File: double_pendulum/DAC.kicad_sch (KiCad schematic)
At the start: 16 parts, among them U4 MCP4922-E_P, U5 TL072, U7 MCP4922-E_P, U9 TL072

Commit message: double pendulum 4ms package path update
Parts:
- U5, U9: footprint PCM_4ms_Package_SSOP:TSSOP-8_4.4x3mm_Pitch0.65mm -> 4ms_Package_SSOP:TSSOP-8_4.4x3mm_Pitch0.65mm
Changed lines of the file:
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@@
 			)
 		)
-		(property "Footprint" "PCM_4ms_Package_SSOP:TSSOP-8_4.4x3mm_Pitch0.65mm"
+		(property "Footprint" "4ms_Package_SSOP:TSSOP-8_4.4x3mm_Pitch0.65mm"
 			(at 205.74 33.02 0)
 			(effects
@@
 			)
 		)
-		(property "Footprint" "PCM_4ms_Package_SSOP:TSSOP-8_4.4x3mm_Pitch0.65mm"
+		(property "Footprint" "4ms_Package_SSOP:TSSOP-8_4.4x3mm_Pitch0.65mm"
 			(at 205.74 59.69 0)
 			(effects
@@
 			)
 		)
-		(property "Footprint" "PCM_4ms_Package_SSOP:TSSOP-8_4.4x3mm_Pitch0.65mm"
+		(property "Footprint" "4ms_Package_SSOP:TSSOP-8_4.4x3mm_Pitch0.65mm"
 			(at 204.47 82.55 0)
 			(effects
@@
 			)
 		)
-		(property "Footprint" "PCM_4ms_Package_SSOP:TSSOP-8_4.4x3mm_Pitch0.65mm"
+		(property "Footprint" "4ms_Package_SSOP:TSSOP-8_4.4x3mm_Pitch0.65mm"
 			(at 204.47 109.22 0)
 			(effects

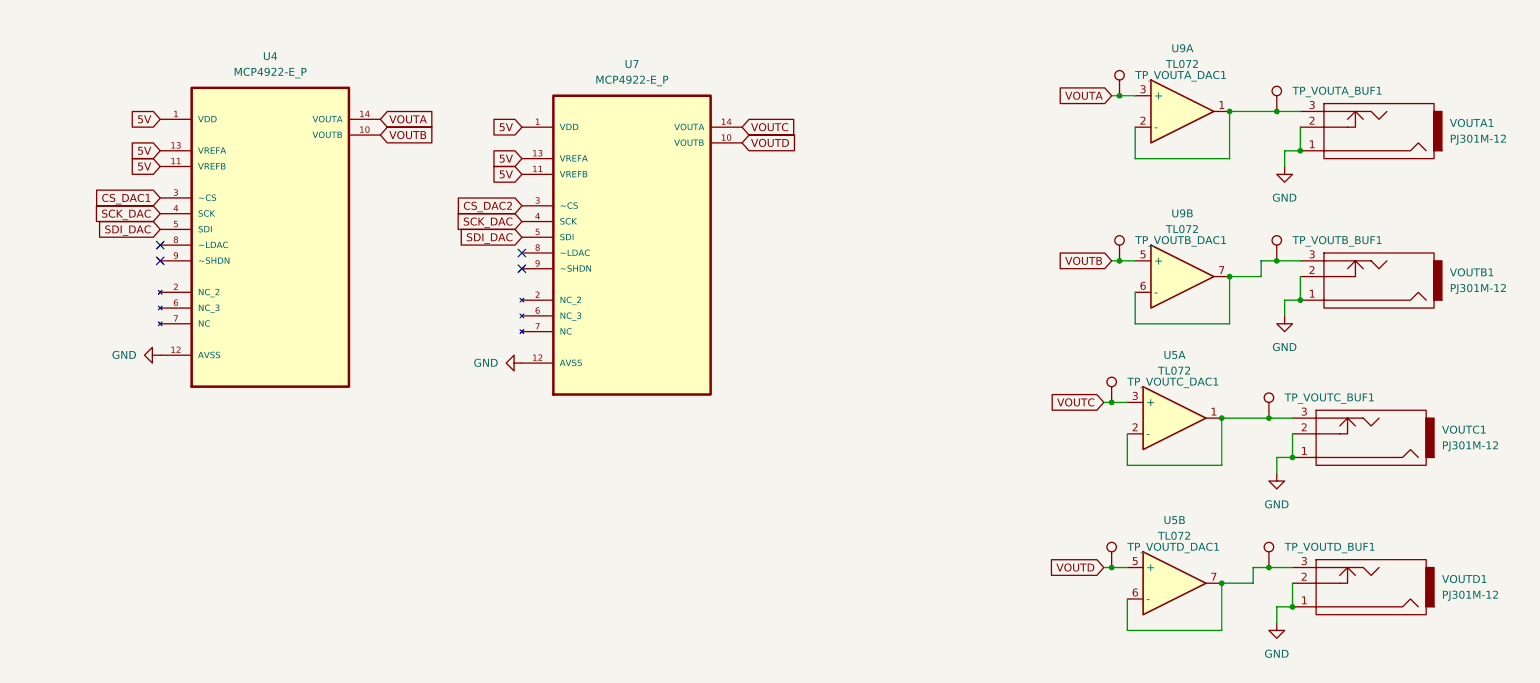
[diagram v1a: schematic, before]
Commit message: Finished schematic and layout of the double pendulum
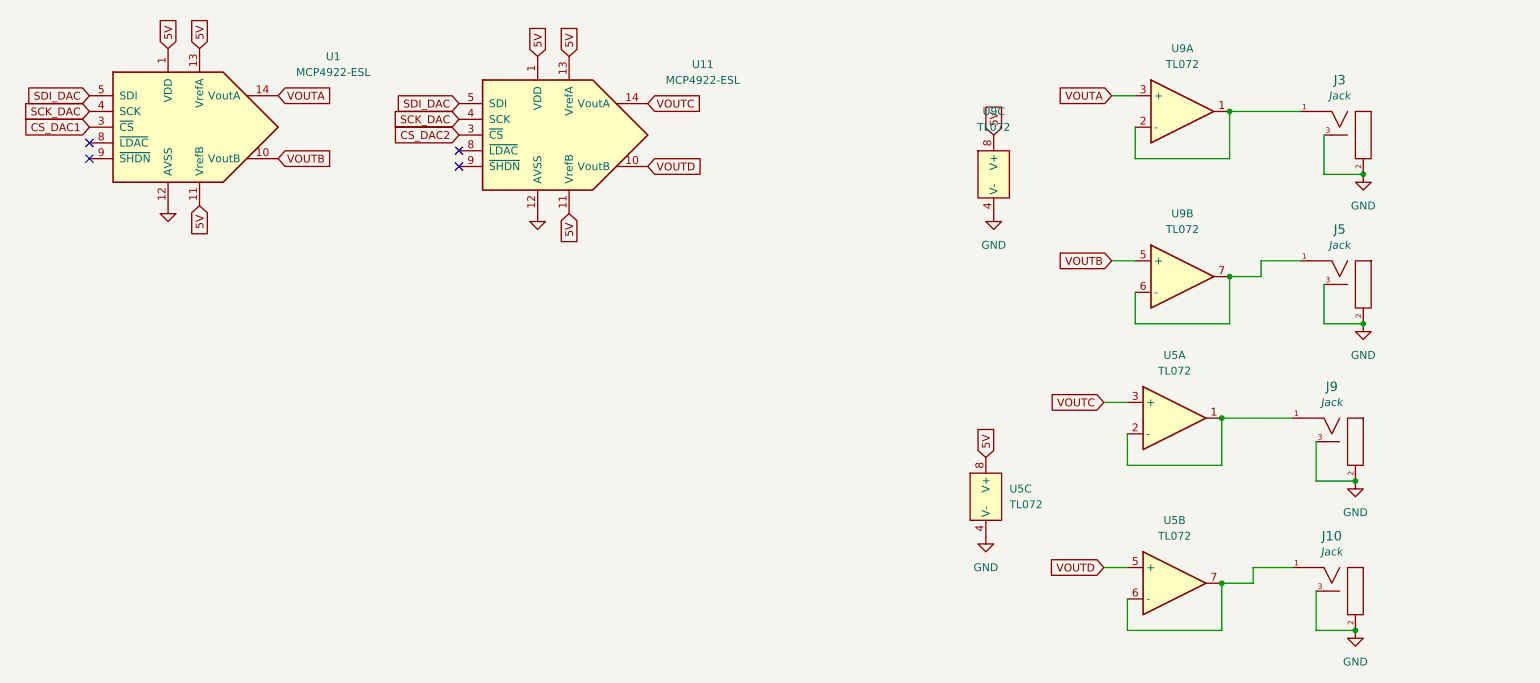
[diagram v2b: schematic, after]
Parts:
- removed TP_VOUTA_BUF1, TP_VOUTA_DAC1, TP_VOUTB_BUF1, TP_VOUTB_DAC1, TP_VOUTC_BUF1, TP_VOUTC_DAC1, TP_VOUTD_BUF1, TP_VOUTD_DAC1: TestPoint, TestPoint:TestPoint_Keystone_5005-5009_Compact, symbol Connector:TestPoint
- removed U4, U7: MCP4922-E_P, MCP4922:DIP254P762X533-14, symbol MCP4922:MCP4922-E_P
- removed VOUTA1, VOUTB1, VOUTC1, VOUTD1: PJ301M-12, Eurocad:PJ301M-12, symbol eurocad:PJ301M-12
- added J10, J3, J5, J9: 3.5mm_Mono_Switched_sm, 4ms_Jack:EighthInch_PJ398SM, symbol 4ms_Jack:3.5mm_Mono_Switched_sm
- added U1, U11: MCP4922-ESL, 4ms_Package_SOIC:SOIC-14_3.9x8.65mm_Pitch1.27mm, symbol Analog_DAC:MCP4922-ESL
- added unit 3 of U5
- added unit 3 of U9
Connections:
- net 5V: now also U1.1 (VDD), U1.11 (VrefB), U1.13 (VrefA), U11.1 (VDD), U11.11 (VrefB), U11.13 (VrefA), U5.8 (V+), U9.8 (V+)
- net CS_DAC1: now also U1.3 (~{CS})
- net CS_DAC2: now also U11.3 (~{CS})
- net GND: now also J10.2 (SHEILD), J10.3 (SW), J3.2 (SHEILD), J3.3 (SW), J5.2 (SHEILD), J5.3 (SW), J9.2 (SHEILD), J9.3 (SW), U1.12 (AVSS), U11.12 (AVSS), U5.4 (V-), U9.4 (V-)
- net SCK_DAC: now also U1.4 (SCK), U11.4 (SCK)
- net SDI_DAC: now also U1.5 (SDI), U11.5 (SDI)
- net VOUTA: now also U1.14 (VoutA)
- net VOUTB: now also U1.10 (VoutB)
- net VOUTC: now also U11.14 (VoutA)
- net VOUTD: now also U11.10 (VoutB)
- net at U5.1, U5.2 (-): now also J9.1 (SIG)
- net at U9.6 (-), U9.7: now also J5.1 (SIG)
- net at U9.1, U9.2 (-): now also J3.1 (SIG)
- net at U5.6 (-), U5.7: now also J10.1 (SIG)
